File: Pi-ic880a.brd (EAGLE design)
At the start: 72 x 113 mm, 20 parts, among them Q1 LFXTAL016178, U1 IC880A, U2 BR24G32-3, U3 MCP79412-I/SN

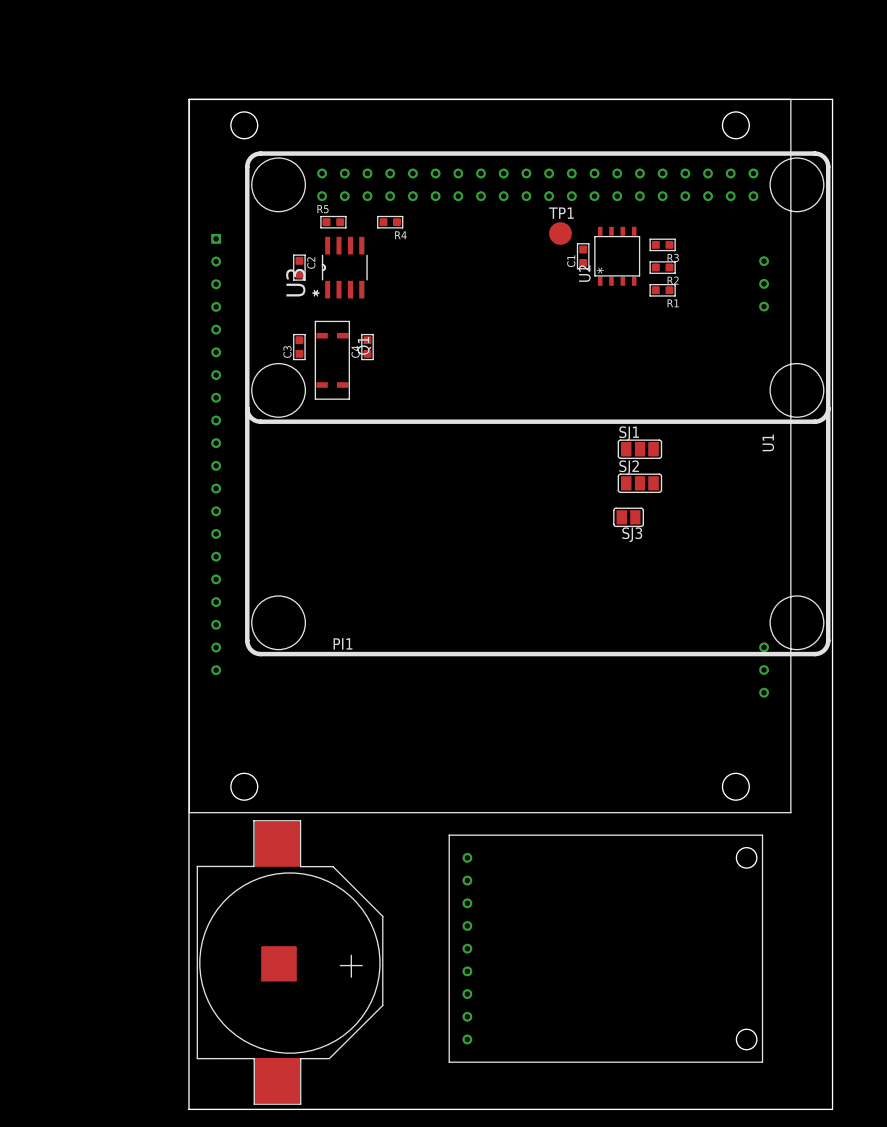
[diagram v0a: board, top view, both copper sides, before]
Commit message: Standalone version of the adafruit GPS module added
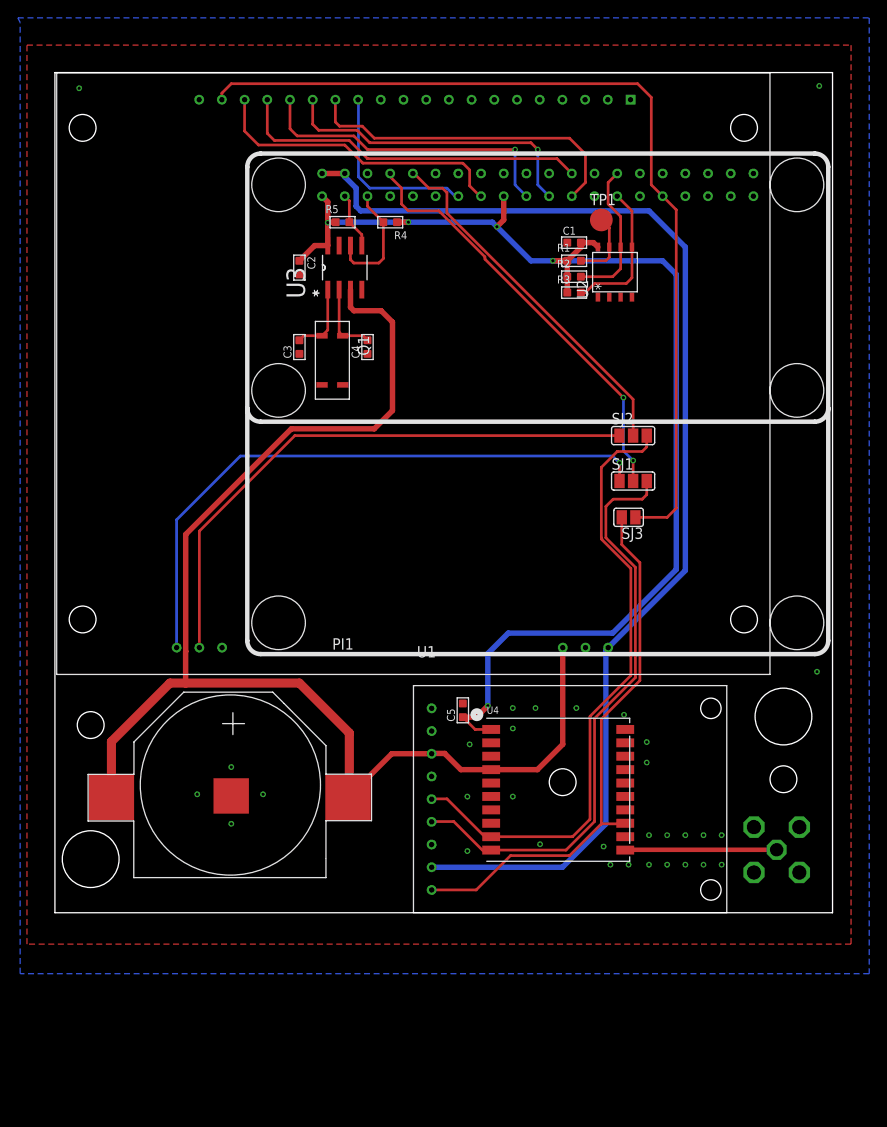
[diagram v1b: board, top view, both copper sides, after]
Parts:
- added C5: 100nf, Seeed-Capacitor-2016:C0603
- added U$2: SMATH, fruit-parts:SMA
- added U4: (no value), fruit-parts:FGPMMOPA6H
- moved U$1 30.1 mm to (-2.98, -7.30), turned to 180 degrees
- moved GPS1 17.2 mm to (36.6, -16.3)
- moved U1 12.6 mm to (19.1, 31.3), turned to 180 degrees
- moved R3 11.3 mm to (37.1, 40.4), turned to 270 degrees
- moved R1 10.4 mm to (37.1, 43.9), turned to 270 degrees
- moved R2 9.96 mm to (37.1, 42.2), turned to 270 degrees
- moved SJ2 5.39 mm to (43.7, 24.4)
- moved TP1 4.82 mm to (40.1, 48.5)
- moved SJ1 3.64 mm to (43.7, 19.3)
- moved C1 1.83 mm to (37.1, 46.0), turned to 90 degrees
- moved U2 1.80 mm to (41.7, 42.7)
- moved R5 1.02 mm to (11.2, 48.3)
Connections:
- new net GPS_ANT: U$2.SIG, U4.P$11
- net +3V3: now also C5.1, U4.P$1
- net ADA_PPS: now also U4.P$13
- net ADA_RXD: now also SJ1.3, U4.P$10; no longer SJ1.1
- net ADA_TXD: now also SJ2.3, U4.P$9; no longer SJ2.1
- net GND: now also C5.2, U$2.GND1, U$2.GND2, U$2.GND3, U$2.GND4, U4.P$12, U4.P$19, U4.P$3, U4.P$8
- net UBLOX_RXD: now also SJ1.1; no longer SJ1.3
- net UBLOX_TXD: now also SJ2.1; no longer SJ2.3
- net VBAT: now also U4.P$4
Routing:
- net VBAT: track 0.00 -> 146.8 mm
- net +3V3: track 0.00 -> 137.9 mm, vias 0 -> 5
- net +5V: track 0.00 -> 135.2 mm
- net PPS: track 0.00 -> 102.2 mm
- net ADA_TXD: track 0.00 -> 70.2 mm
- net UBLOX_RXD: track 0.00 -> 69.2 mm, vias 0 -> 1
- net ADA_RXD: track 0.00 -> 66.0 mm
- net UBLOX_TXD: track 0.00 -> 64.5 mm
- net ADA_PPS: track 0.00 -> 62.6 mm
- net PI_TXD: track 0.00 -> 47.7 mm, vias 0 -> 2
- net PI_RXD: track 0.00 -> 40.5 mm
- net SX1301_NSS: track 0.00 -> 39.7 mm
- net SCLK: track 0.00 -> 37.3 mm
- net MOSI: track 0.00 -> 35.1 mm, vias 0 -> 1
- net MISO: track 0.00 -> 34.8 mm, vias 0 -> 1
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- added copper zone on layer 1, net GND
- added copper zone on layer 16, net GND
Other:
- board size 72 x 113 mm -> 87 x 94 mm

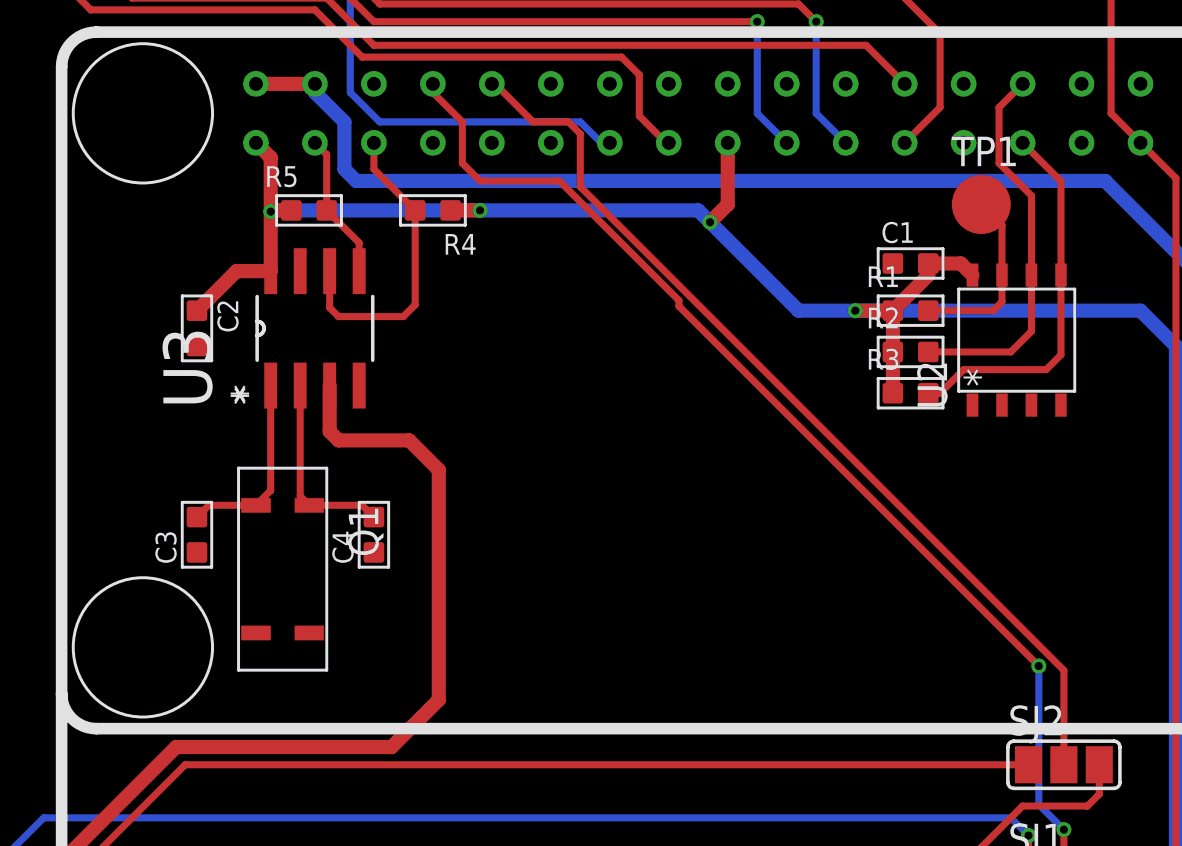
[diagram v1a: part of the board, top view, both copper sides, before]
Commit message: Now uses ds3231 as RTC
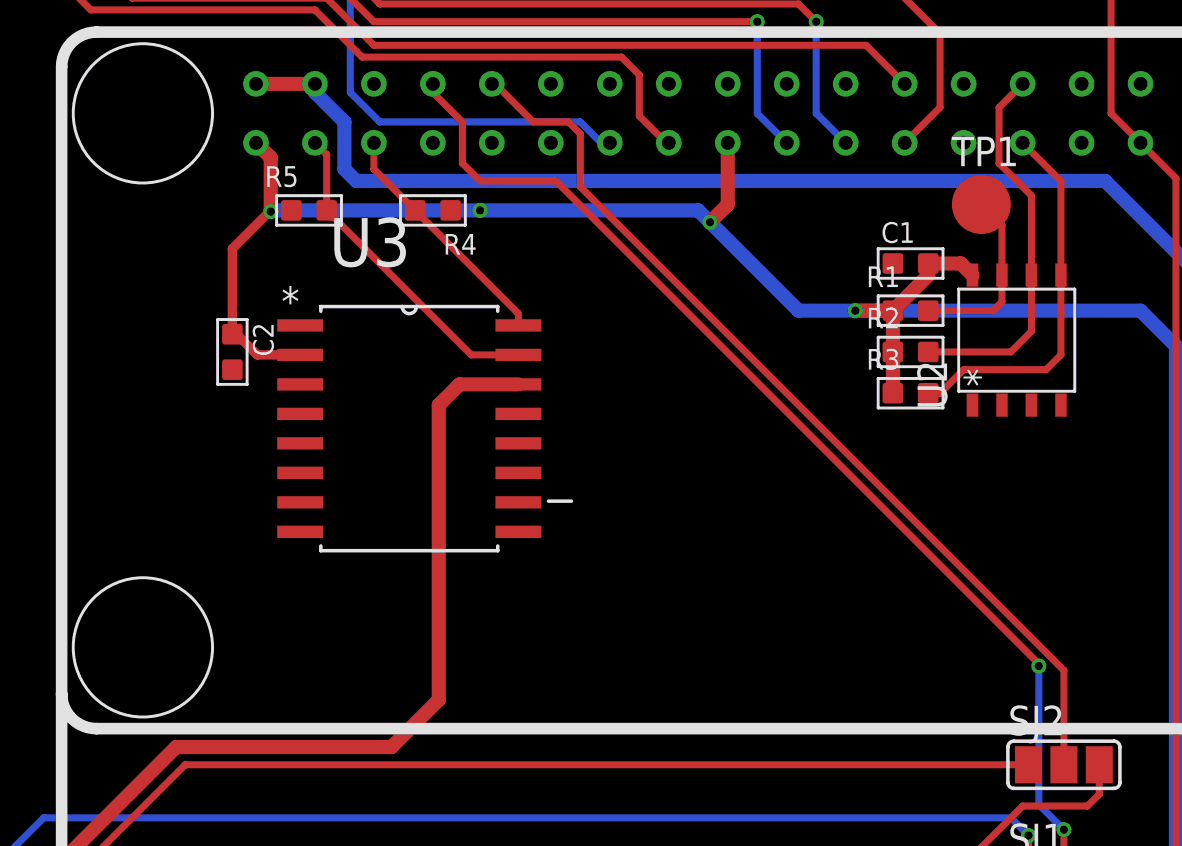
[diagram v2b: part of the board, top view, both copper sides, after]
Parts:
- removed C3, C4: 10pf, Seeed-Capacitor-2016:C0603
- removed Q1: LFXTAL016178, fruit-parts:85SMX
- U3: value MCP79412-I/SN -> DS3231SN; device farnell-parts:SOIC127P600X175-8N -> imported-parts:SOIC127P1032X265-16N
- moved U3 5.93 mm to (15.5, 38.9), turned to 0 degrees
- moved C2 1.83 mm to (7.87, 42.2)
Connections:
- removed net X1: C3.2, Q1.1, U3.1
- removed net X2: C4.2, Q1.4, U3.2
- net +3V3: now also U3.2; no longer U3.8
- net GND: now also U3.10, U3.11, U3.12, U3.13, U3.5, U3.6, U3.7, U3.8, U3.9; no longer C3.1, C4.1, U3.4
- net SCL: now also U3.16; no longer U3.6
- net SDA: now also U3.15; no longer U3.5
- net VBAT: now also U3.14; no longer U3.3
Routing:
- net X2: track 8.31 -> 0.00 mm
- net X1: track 8.17 -> 0.00 mm
- net SDA: track 6.32 -> 14.0 mm
- net SCL: track 13.3 -> 10.4 mm
- net +3V3: track 137.9 -> 138.7 mm
- net VBAT: track 146.8 -> 146.0 mm

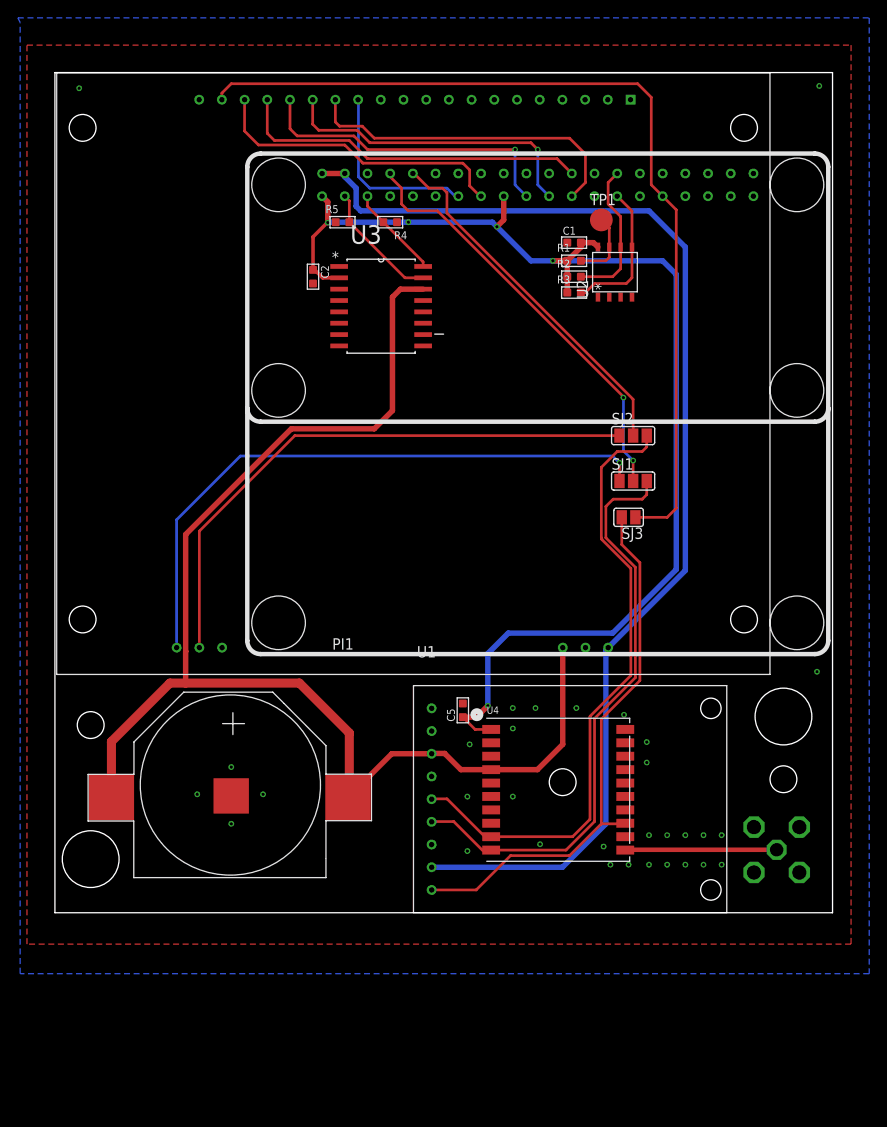
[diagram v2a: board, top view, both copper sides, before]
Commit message: DHT22 added now fully laid out and ready for final check through
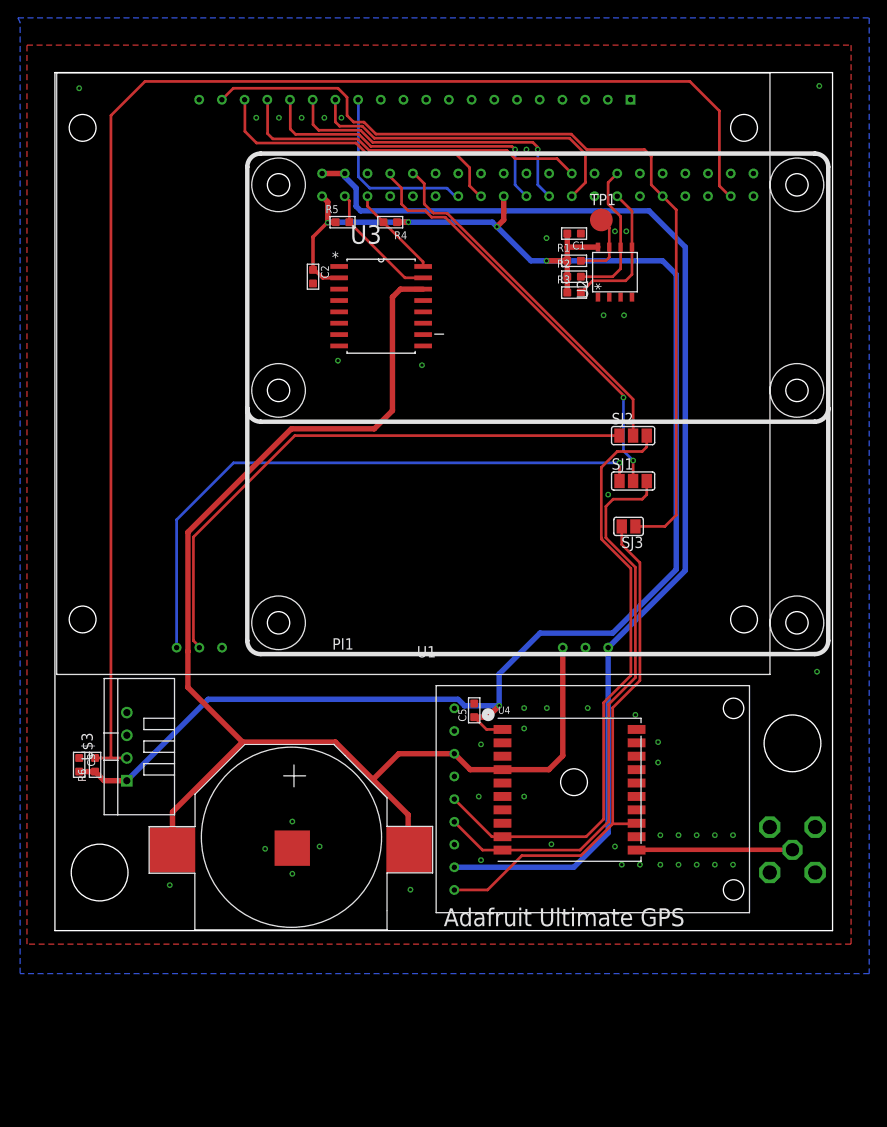
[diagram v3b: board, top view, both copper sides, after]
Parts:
- added C3: 100pf, Seeed-Capacitor:C0603
- added R6: 10K, Seeed-Resistor:R0603
- added U$3: TEMP-HUM-SENSOR-DHT22, fruit-parts:TEMP-HUM-SENSOR-DHT22
- moved U$1 8.99 mm to (3.85, -13.1)
- moved GPS1 2.54 mm to (39.2, -16.3)
- moved U$2 1.77 mm to (61.5, -22.0)
- moved U4 1.27 mm to (36.6, -15.2)
- moved C5 1.27 mm to (25.9, -6.35)
- moved C1 1.02 mm to (37.1, 47.0), turned to 270 degrees
- moved SJ3 1.02 mm to (43.2, 14.2)
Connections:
- new net DHT22: PI1.37, R6.1, U$3.2
- net +3V3: now also C3.2, R6.2, U$3.1
- net GND: now also C3.1, U$3.4
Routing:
- net DHT22: track 0.00 -> 156.6 mm
- net +3V3: track 138.7 -> 192.1 mm
- net PPS: track 102.2 -> 99.3 mm
- net ADA_PPS: track 62.6 -> 59.7 mm
- net VBAT: track 146.0 -> 148.1 mm
- net +5V: track 135.2 -> 133.4 mm
- net ADA_RXD: track 66.0 -> 64.4 mm
- net ADA_TXD: track 70.2 -> 69.3 mm
- net UBLOX_RXD: track 69.2 -> 68.5 mm
- net UBLOX_TXD: track 64.5 -> 65.0 mm
- net GPS_ANT: track 17.0 -> 17.5 mm
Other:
- board size 87 x 94 mm -> 87 x 96 mm
- board text added: "Adafruit Ultimate GPS"
- board text added: "EEPROM WP"
- board text added: "Module"
- board text added: "PPS Link"
- board text added: "RX"
- board text added: "SMD"
- board text added: "TX"
- board text added: "University of Southampton"
- board text added: "V1.0"

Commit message: Added jumpers for BAT more work on labelling added test pads for VBAT
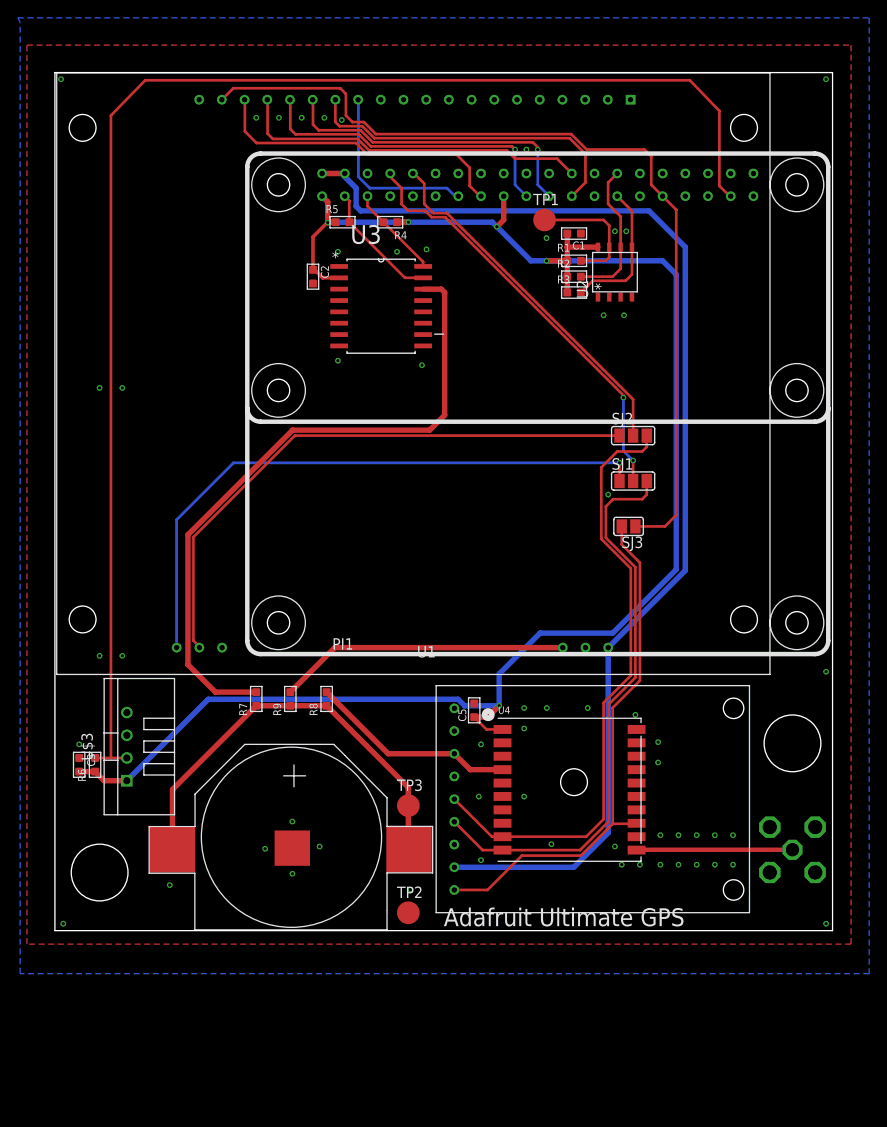
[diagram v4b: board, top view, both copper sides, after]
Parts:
- added R7, R8, R9: 0R, Seeed-Resistor:R0603
- added TP2, TP3: TPB2,54, testpad:B2,54
- moved TP1 6.35 mm to (33.8, 48.5)
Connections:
- new net VBAT_GPS: GPS1.3, R8.1, U4.P$4
- new net VBAT_IC880: R9.1, U1.23
- new net VBAT_RTC: R7.1, U3.14
- net GND: now also TP2.TP
- net VBAT: now also R7.2, R8.2, R9.2, TP3.TP; no longer GPS1.3, U1.23, U3.14, U4.P$4
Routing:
- net VBAT: track 148.1 -> 47.9 mm
- net VBAT_RTC: track 0.00 -> 74.0 mm
- net VBAT_IC880: track 0.00 -> 32.5 mm
- net VBAT_GPS: track 0.00 -> 23.3 mm
- net WP: track 7.89 -> 14.4 mm
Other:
- board text added: "Backup Batt"
- board text added: "GPS"
- board text added: "RTC"
- board text added: "Seperate"
- board text added: "UBX"
- board text added: "UBlox"
- board text removed: "Module"
- board text removed: "SMD"

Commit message: After adding all other GPIO
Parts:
- moved C2 1.08 mm to (7.11, 42.9), turned to 270 degrees
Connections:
- new net !GPS_RESET: PI1.13, U1.3
- new net EN_GPS: PI1.16, U1.5
- new net SP_VALID: PI1.18, U1.4
- new net SX1301_GPIO0: PI1.40, U1.7
- new net SX1301_GPIO1: PI1.38, U1.8
- new net SX1301_GPIO2: PI1.32, U1.10
- new net SX1301_GPIO3: PI1.36, U1.9
- new net SX1301_GPIO4: PI1.29, U1.11
- net SX1301_RST: now also PI1.11; no longer PI1.13
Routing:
- net SX1301_GPIO3: track 0.00 -> 34.4 mm
- net SX1301_GPIO1: track 0.00 -> 34.1 mm
- net SX1301_GPIO4: track 0.00 -> 33.8 mm, vias 0 -> 1
- net SX1301_GPIO0: track 0.00 -> 33.5 mm
- net SX1301_GPIO2: track 0.00 -> 32.2 mm
- net !GPS_RESET: track 0.00 -> 21.7 mm
- net SP_VALID: track 0.00 -> 13.4 mm
- net EN_GPS: track 0.00 -> 11.0 mm
- net DHT22: track 156.8 -> 167.3 mm
- net SX1301_RST: track 20.7 -> 18.2 mm
- net PPS: track 99.5 -> 98.6 mm
- net +3V3: track 192.1 -> 191.3 mm
